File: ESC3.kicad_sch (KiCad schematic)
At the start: 35 parts, among them J11 SWD1, J12 MOTOR1, Q10 XRS306D, Q8 XRS306D, Q9 XRS306D, U11 STM32G071GBUxN, U12 DRV8300D

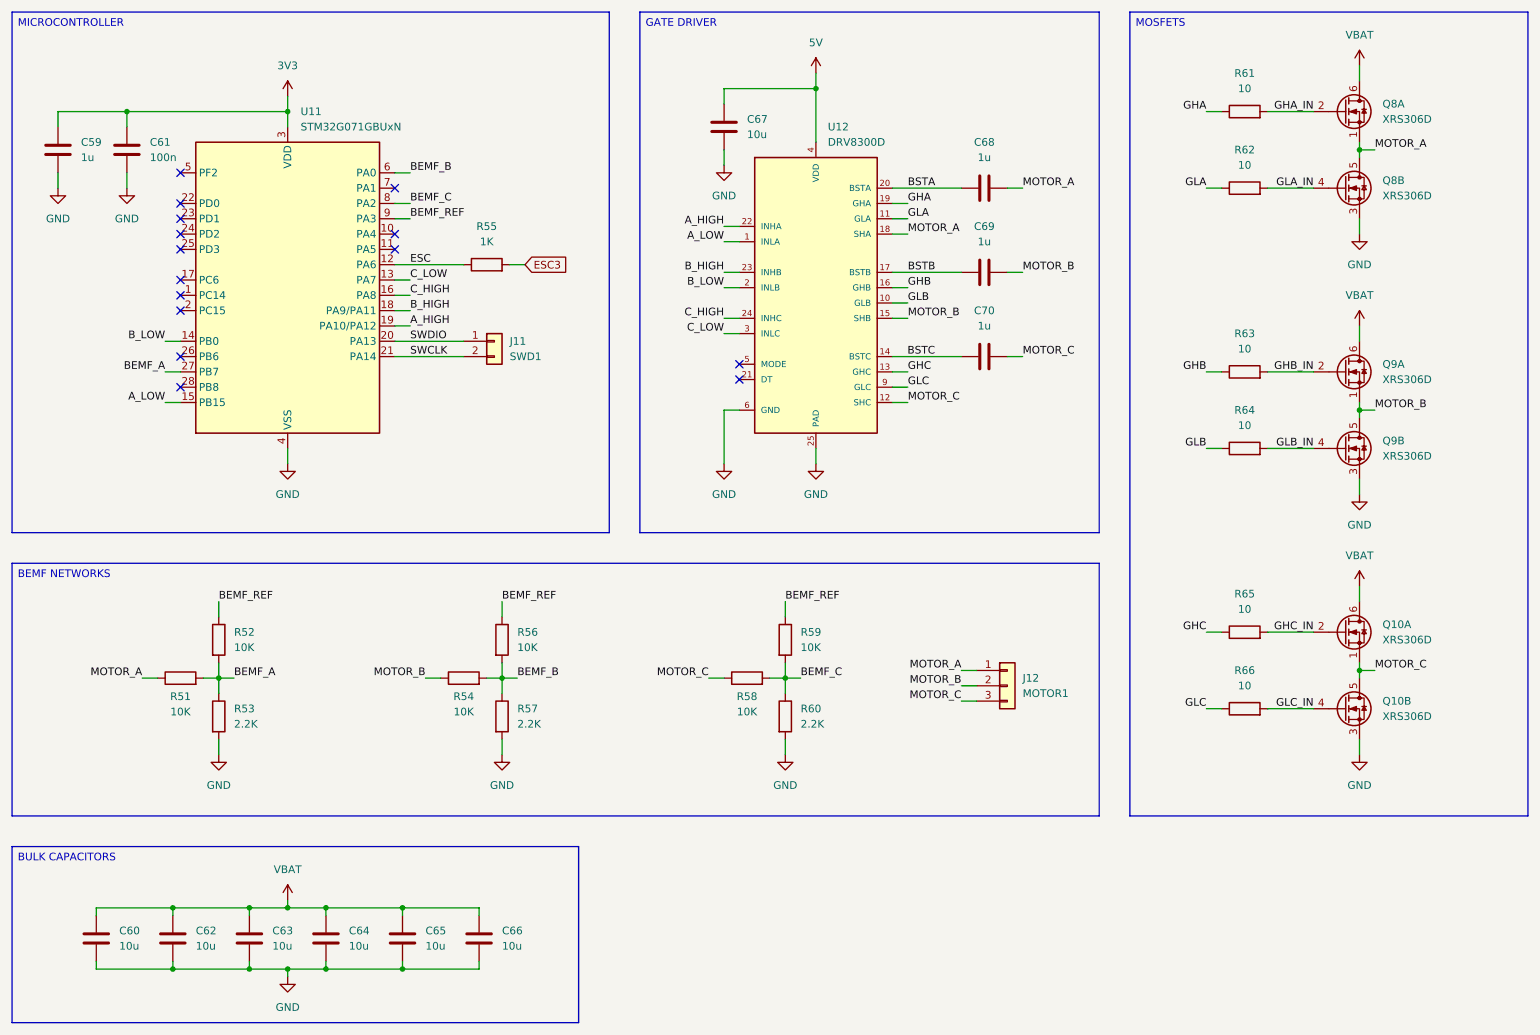
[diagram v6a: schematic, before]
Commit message: Initial layout
Completed an initial layout of the main components.

TODO
Route the ESCs and check the result.
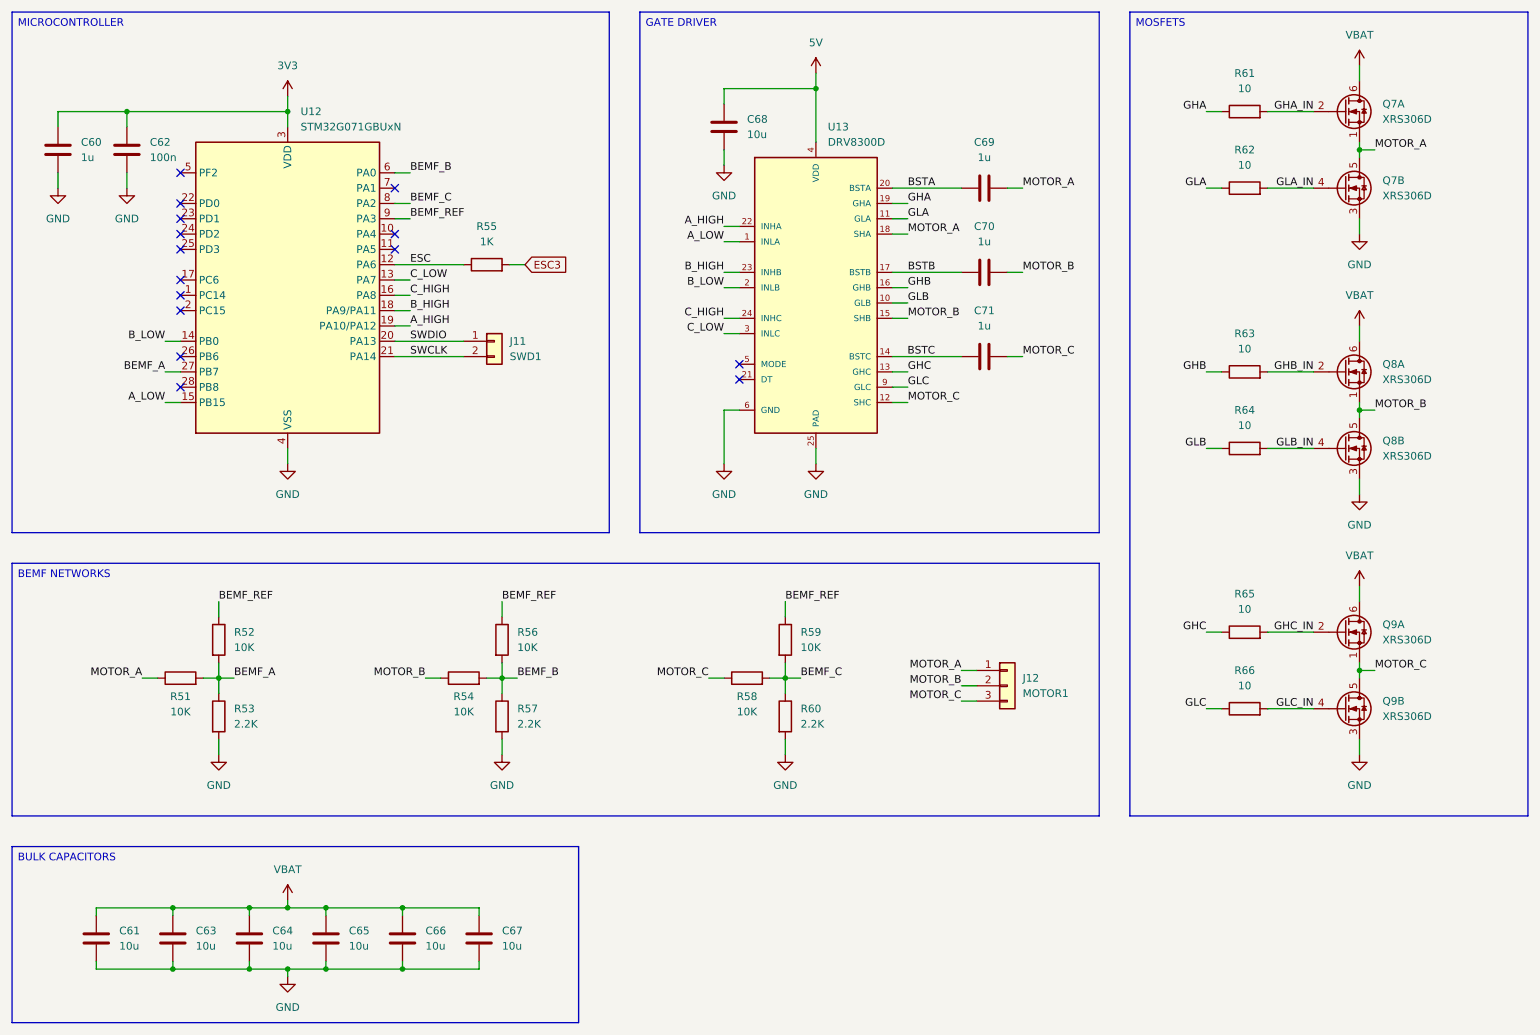
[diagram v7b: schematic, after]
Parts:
- renumbered C59 to C60, C60 to C61, C61 to C62, C62 to C63, C63 to C64, C64 to C65, C65 to C66, C66 to C67, C67 to C68, C68 to C69, C69 to C70, C70 to C71, Q8 to Q7, Q9 to Q8, Q10 to Q9, U11 to U12, U12 to U13

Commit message: Settings and ESC layout
Updated the PCB configuration options for manufacturing.
Completed the initial ESC layout.

TODO:
Replicate ESC layout.
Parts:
- J12: footprint Custom_Parts:PAD_3_SQUARE_SOLID_2.5x2.5mm_P4.0mm -> Custom_Parts:PAD_3_SQUARE_SOLID_2.5x2.5mm_P4.0mm_MOTOR
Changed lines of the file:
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@@
 			)
 		)
-		(property "Footprint" "Custom_Parts:PAD_3_SQUARE_SOLID_2.5x2.5mm_P4.0mm"
+		(property "Footprint" "Custom_Parts:PAD_3_SQUARE_SOLID_2.5x2.5mm_P4.0mm_MOTOR"
 			(at 187.96 134.62 0)
 			(effects
